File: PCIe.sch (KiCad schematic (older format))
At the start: 16 parts, among them J2 Bus_PCI_Express_Mini, U1 MIMX8MM6DVTLZAA

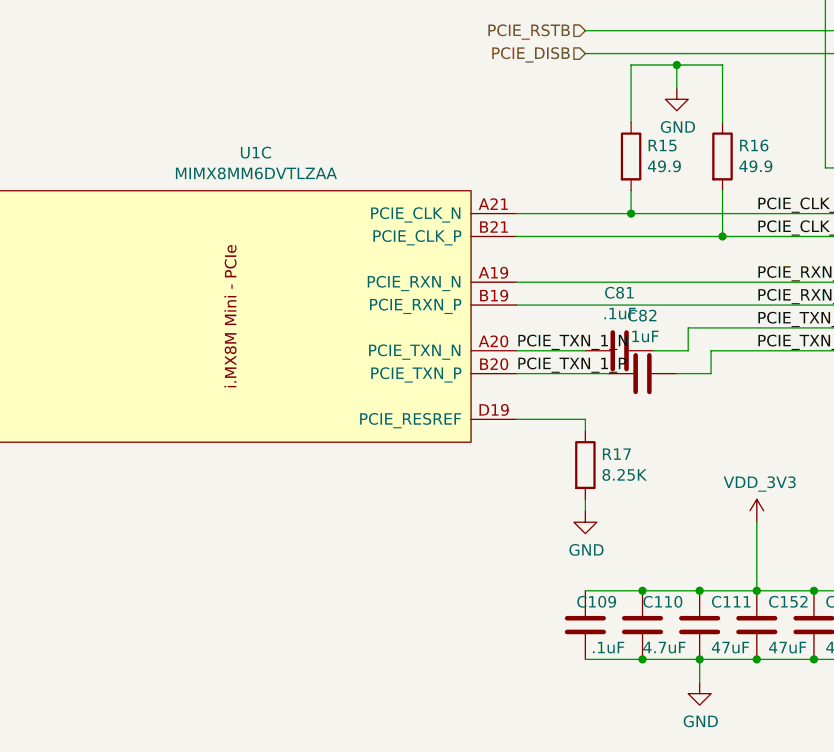
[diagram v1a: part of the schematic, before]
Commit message: Complete entry of bom
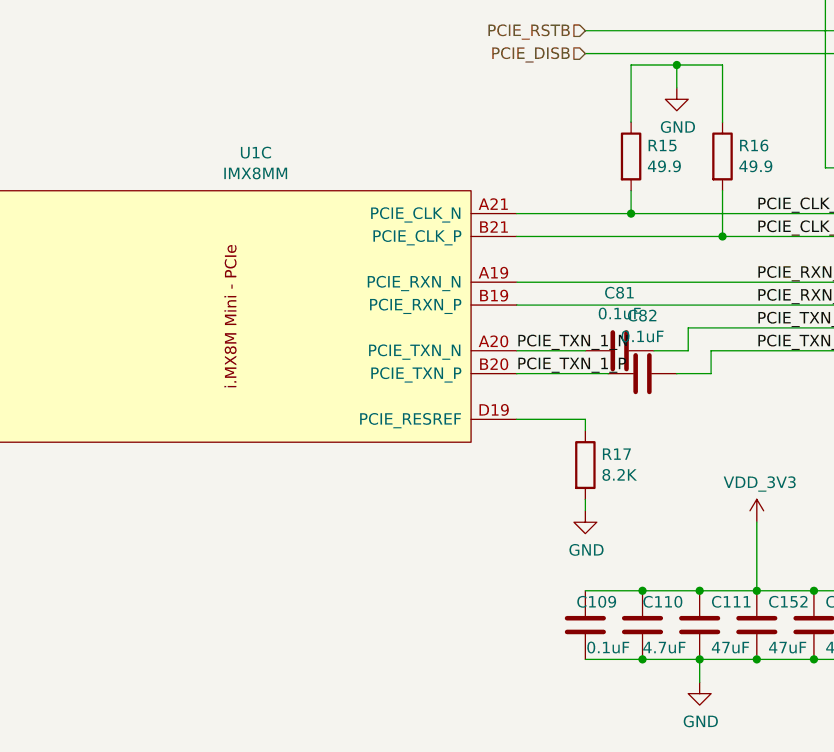
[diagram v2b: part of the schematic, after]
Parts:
- C109, C81, C82: value .1uF -> 0.1uF; footprint Resistor_SMD:R_0201_0603Metric -> Capacitor_SMD:C_0201_0603Metric; Mfgr (none) -> Murata; Part (none) -> GRM033C80J104KE15D; Vendorpart (none) -> 490-10390-1-ND
- C110, C156: Mfgr (none) -> Murata; Part (none) -> GRM155C80J475MEAAD; Vendorpart (none) -> 490-14458-1-ND
- C111, C152, C153, C154, C155: Mfgr (none) -> Murata; Part (none) -> GRM21BC80G476ME15L; Vendorpart (none) -> 490-9954-1-ND
- C157: Mfgr (none) -> Murata; Part (none) -> GRM155C80J106ME11D; Vendorpart (none) -> 490-13233-1-ND
- J2: Mfgr (none) -> TE; Part (none) -> 1775838-2; Vendorpart (none) -> A123340CT-ND
- R15, R16: Mfgr (none) -> Yageo; Part (none) -> RC0201FR-0749R9L; Vendorpart (none) -> YAG2702CT-ND
- R17: value 8.25K -> 8.2K; Mfgr (none) -> Yageo; Part (none) -> RC0201FR-078K2L; Vendorpart (none) -> YAG2353CT-ND
- U1: value MIMX8MM6DVTLZAA -> IMX8MM; Mfgr (none) -> NXP; Part (none) -> MIMX8MM6CVTKZAA; Vendorpart (none) -> 568-15276-ND
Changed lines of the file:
@@
 F 2 "mxenc:1775838-2-NPTH" H 7350 3750 50  0001 C CNN
 F 3 "~" H 7200 2600 50  0001 C CNN
+F 4 "TE" H 7350 3750 50  0001 C CNN "Mfgr"
+F 5 "1775838-2" H 7350 3750 50  0001 C CNN "Part"
+F 6 "A123340CT-ND" H 7350 3750 50  0001 C CNN "Vendorpart"
 	1    7350 3750
 	1    0    0    1
@@
 P 3700 6150
 F 0 "U1" H 3808 9015 50  0000 C CNN
-F 1 "MIMX8MM6DVTLZAA" H 3808 8924 50  0000 C CNN
+F 1 "IMX8MM" H 3808 8924 50  0000 C CNN
 F 2 "mxenc:BGA-729_27x27_14.0x14.0mm" H 3950 8900 50  0001 C CNN
 F 3 "" H 2950 8900 50  0001 C CNN
+F 4 "NXP" H 3700 6150 50  0001 C CNN "Mfgr"
+F 5 "MIMX8MM6CVTKZAA" H 3700 6150 50  0001 C CNN "Part"
+F 6 "568-15276-ND" H 3700 6150 50  0001 C CNN "Vendorpart"
 	3    3700 6150
 	1    0    0    -1
@@
 P 5250 4650
 F 0 "R17" H 5320 4696 50  0000 L CNN
-F 1 "8.25K" H 5320 4605 50  0000 L CNN
+F 1 "8.2K" H 5320 4605 50  0000 L CNN
 F 2 "Resistor_SMD:R_0201_0603Metric" V 5180 4650 50  0001 C CNN
 F 3 "~" H 5250 4650 50  0001 C CNN
+F 4 "Yageo" H 5250 4650 50  0001 C CNN "Mfgr"
+F 5 "RC0201FR-078K2L" H 5250 4650 50  0001 C CNN "Part"
+F 6 "YAG2353CT-ND" H 5250 4650 50  0001 C CNN "Vendorpart"
 	1    5250 4650
 	1    0    0    -1
@@
 F 2 "Resistor_SMD:R_0201_0603Metric" V 5380 3300 50  0001 C CNN
 F 3 "~" H 5450 3300 50  0001 C CNN
+F 4 "Yageo" H 5450 3300 50  0001 C CNN "Mfgr"
+F 5 "RC0201FR-0749R9L" H 5450 3300 50  0001 C CNN "Part"
+F 6 "YAG2702CT-ND" H 5450 3300 50  0001 C CNN "Vendorpart"
 	1    5450 3300
 	1    0    0    -1
@@
 F 2 "Resistor_SMD:R_0201_0603Metric" V 5780 3300 50  0001 C CNN
 F 3 "~" H 5850 3300 50  0001 C CNN
+F 4 "Yageo" H 5850 3300 50  0001 C CNN "Mfgr"
+F 5 "RC0201FR-0749R9L" H 5850 3300 50  0001 C CNN "Part"
+F 6 "YAG2702CT-ND" H 5850 3300 50  0001 C CNN "Vendorpart"
 	1    5850 3300
 	1    0    0    -1
@@
 F 2 "Capacitor_SMD:C_0402_1005Metric" H 7938 5200 50  0001 C CNN
 F 3 "~" H 7900 5350 50  0001 C CNN
+F 4 "Murata" H 7900 5350 50  0001 C CNN "Mfgr"
+F 5 "GRM155C80J475MEAAD" H 7900 5350 50  0001 C CNN "Part"
+F 6 "490-14458-1-ND" H 7900 5350 50  0001 C CNN "Vendorpart"
 	1    7900 5350
 	1    0    0    -1
@@
 F 2 "Capacitor_SMD:C_0402_1005Metric" H 8188 5200 50  0001 C CNN
 F 3 "~" H 8150 5350 50  0001 C CNN
+F 4 "Murata" H 8150 5350 50  0001 C CNN "Mfgr"
+F 5 "GRM155C80J106ME11D" H 8150 5350 50  0001 C CNN "Part"
+F 6 "490-13233-1-ND" H 8150 5350 50  0001 C CNN "Vendorpart"
 	1    8150 5350
 	1    0    0    -1
@@
 F 2 "Capacitor_SMD:C_0805_2012Metric" H 6788 5200 50  0001 C CNN
 F 3 "~" H 6750 5350 50  0001 C CNN
+F 4 "Murata" H 6750 5350 50  0001 C CNN "Mfgr"
+F 5 "GRM21BC80G476ME15L" H 6750 5350 50  0001 C CNN "Part"
+F 6 "490-9954-1-ND" H 6750 5350 50  0001 C CNN "Vendorpart"
 	1    6750 5350
 	1    0    0    -1
@@
 F 2 "Capacitor_SMD:C_0805_2012Metric" H 6538 5200 50  0001 C CNN
 F 3 "~" H 6500 5350 50  0001 C CNN
+F 4 "Murata" H 6500 5350 50  0001 C CNN "Mfgr"
+F 5 "GRM21BC80G476ME15L" H 6500 5350 50  0001 C CNN "Part"
+F 6 "490-9954-1-ND" H 6500 5350 50  0001 C CNN "Vendorpart"
 	1    6500 5350
 	1    0    0    -1
@@
 F 2 "Capacitor_SMD:C_0805_2012Metric" H 6288 5200 50  0001 C CNN
 F 3 "~" H 6250 5350 50  0001 C CNN
+F 4 "Murata" H 6250 5350 50  0001 C CNN "Mfgr"
+F 5 "GRM21BC80G476ME15L" H 6250 5350 50  0001 C CNN "Part"
+F 6 "490-9954-1-ND" H 6250 5350 50  0001 C CNN "Vendorpart"
 	1    6250 5350
 	1    0    0    -1
@@
 F 2 "Capacitor_SMD:C_0805_2012Metric" H 6038 5200 50  0001 C CNN
 F 3 "~" H 6000 5350 50  0001 C CNN
+F 4 "Murata" H 6000 5350 50  0001 C CNN "Mfgr"
+F 5 "GRM21BC80G476ME15L" H 6000 5350 50  0001 C CNN "Part"
+F 6 "490-9954-1-ND" H 6000 5350 50  0001 C CNN "Vendorpart"
 	1    6000 5350
 	1    0    0    -1
@@
 F 2 "Capacitor_SMD:C_0805_2012Metric" H 5788 5200 50  0001 C CNN
 F 3 "~" H 5750 5350 50  0001 C CNN
+F 4 "Murata" H 5750 5350 50  0001 C CNN "Mfgr"
+F 5 "GRM21BC80G476ME15L" H 5750 5350 50  0001 C CNN "Part"
+F 6 "490-9954-1-ND" H 5750 5350 50  0001 C CNN "Vendorpart"
 	1    5750 5350
 	1    0    0    -1
@@
 F 2 "Capacitor_SMD:C_0402_1005Metric" H 5538 5200 50  0001 C CNN
 F 3 "~" H 5500 5350 50  0001 C CNN
+F 4 "Murata" H 5500 5350 50  0001 C CNN "Mfgr"
+F 5 "GRM155C80J475MEAAD" H 5500 5350 50  0001 C CNN "Part"
+F 6 "490-14458-1-ND" H 5500 5350 50  0001 C CNN "Vendorpart"
 	1    5500 5350
 	1    0    0    -1
@@
 P 5250 5350
 F 0 "C109" H 5300 5450 50  0000 C CNN
-F 1 ".1uF" H 5350 5250 50  0000 C CNN
-F 2 "Resistor_SMD:R_0201_0603Metric" H 5288 5200 50  0001 C CNN
+F 1 "0.1uF" H 5350 5250 50  0000 C CNN
+F 2 "Capacitor_SMD:C_0201_0603Metric" H 5288 5200 50  0001 C CNN
 F 3 "~" H 5250 5350 50  0001 C CNN
+F 4 "Murata" H 5250 5350 50  0001 C CNN "Mfgr"
+F 5 "GRM033C80J104KE15D" H 5250 5350 50  0001 C CNN "Part"
+F 6 "490-10390-1-ND" H 5250 5350 50  0001 C CNN "Vendorpart"
 	1    5250 5350
 	1    0    0    -1
@@
 P 5500 4250
 F 0 "C82" V 5248 4250 50  0000 C CNN
-F 1 ".1uF" V 5339 4250 50  0000 C CNN
-F 2 "Resistor_SMD:R_0201_0603Metric" H 5538 4100 50  0001 C CNN
+F 1 "0.1uF" V 5339 4250 50  0000 C CNN
+F 2 "Capacitor_SMD:C_0201_0603Metric" H 5538 4100 50  0001 C CNN
 F 3 "~" H 5500 4250 50  0001 C CNN
+F 4 "Murata" H 5500 4250 50  0001 C CNN "Mfgr"
+F 5 "GRM033C80J104KE15D" H 5500 4250 50  0001 C CNN "Part"
+F 6 "490-10390-1-ND" H 5500 4250 50  0001 C CNN "Vendorpart"
 	1    5500 4250
 	0    1    1    0
@@
 P 5400 4150
 F 0 "C81" V 5148 4150 50  0000 C CNN
-F 1 ".1uF" V 5239 4150 50  0000 C CNN
-F 2 "Resistor_SMD:R_0201_0603Metric" H 5438 4000 50  0001 C CNN
+F 1 "0.1uF" V 5239 4150 50  0000 C CNN
+F 2 "Capacitor_SMD:C_0201_0603Metric" H 5438 4000 50  0001 C CNN
 F 3 "~" H 5400 4150 50  0001 C CNN
+F 4 "Murata" H 5400 4150 50  0001 C CNN "Mfgr"
+F 5 "GRM033C80J104KE15D" H 5400 4150 50  0001 C CNN "Part"
+F 6 "490-10390-1-ND" H 5400 4150 50  0001 C CNN "Vendorpart"
 	1    5400 4150
 	0    1    1    0

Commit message: Ground mounting pads and route ecspi to expansion
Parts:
- J2: symbol Connector:Bus_PCI_Express_Mini -> mxenc:Bus_PCI_Express_Mini
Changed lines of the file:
@@
 $EndDescr
 $Comp
-L Connector:Bus_PCI_Express_Mini J?
+L mxenc:Bus_PCI_Express_Mini J?
 U 1 1 5D31B8E0
 P 7350 3750

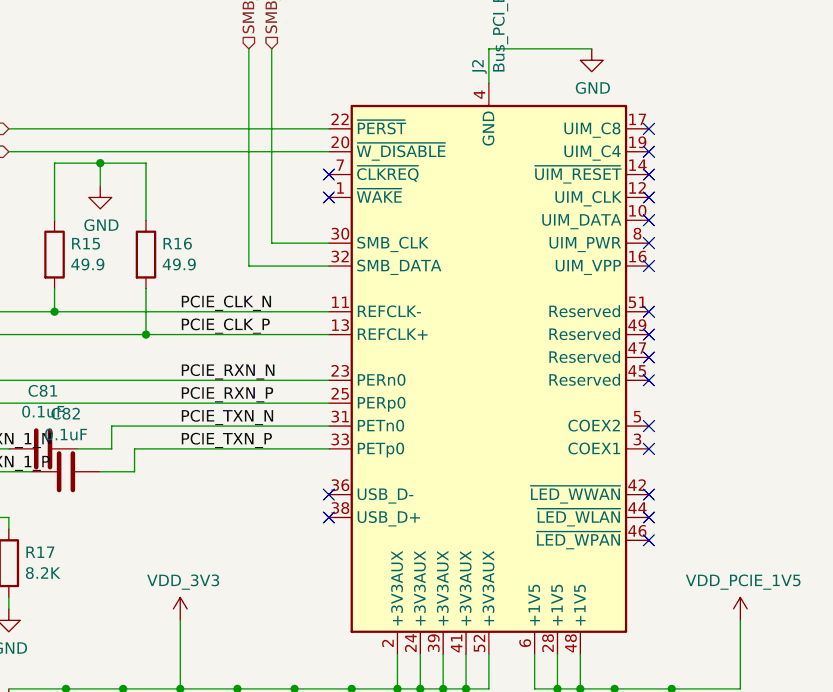
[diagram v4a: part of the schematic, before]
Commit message: UIM and USB routing for PCIE to expansion
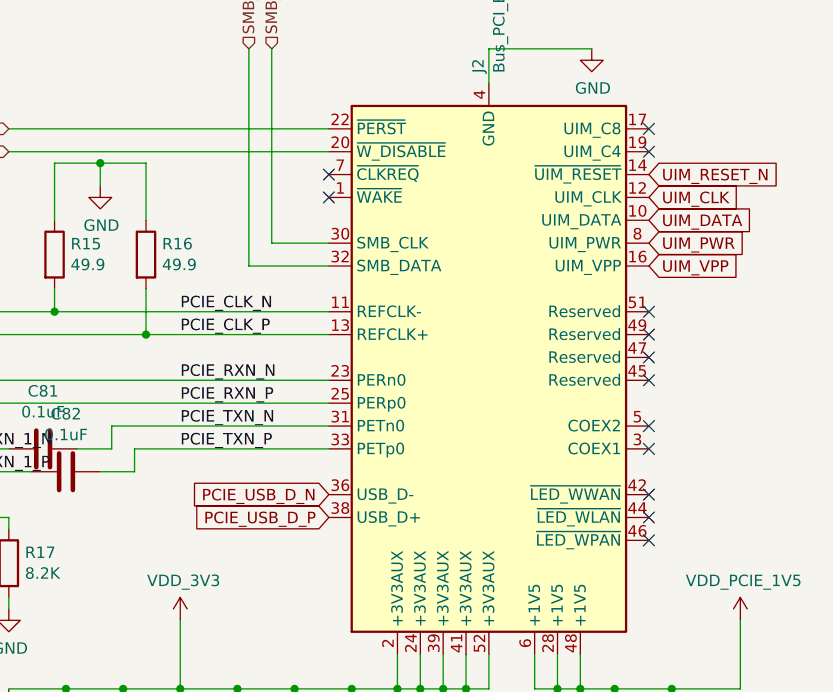
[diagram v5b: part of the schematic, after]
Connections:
- net UIM_DATA: now reaches J2.10 (UIM_DATA)
- net UIM_CLK: now reaches J2.12 (UIM_CLK)
- net UIM_RESET_N: now reaches J2.14 (~UIM_RESET)
- net UIM_VPP: now reaches J2.16 (UIM_VPP)
- net PCIE_USB_D_N: now reaches J2.36 (USB_D-)
- net PCIE_USB_D_P: now reaches J2.38 (USB_D+)
- net UIM_PWR: now reaches J2.8 (UIM_PWR)
- no-connect marks 20 -> 13
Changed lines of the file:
@@
 Wire Wire Line
 	7350 2400 7350 2550
-NoConn ~ 8050 2750
-NoConn ~ 8050 2850
 Wire Wire Line
 	5250 2850 6650 2850
@@
 NoConn ~ 6650 2950
 NoConn ~ 6650 3050
-NoConn ~ 6650 4350
-NoConn ~ 6650 4450
-NoConn ~ 8050 2950
-NoConn ~ 8050 3050
-NoConn ~ 8050 3150
-NoConn ~ 8050 3250
-NoConn ~ 8050 3350
 $Comp
 L power:GND #PWR0198
@@
 Text HLabel 5250 2750 0    50   Input ~ 0
 PCIE_RSTB
+NoConn ~ 8050 2750
+NoConn ~ 8050 2850
+Text GLabel 8050 2950 2    50   Input ~ 0
+UIM_RESET_N
+Text GLabel 8050 3050 2    50   Input ~ 0
+UIM_CLK
+Text GLabel 8050 3150 2    50   Input ~ 0
+UIM_DATA
+Text GLabel 8050 3250 2    50   Input ~ 0
+UIM_PWR
+Text GLabel 8050 3350 2    50   Input ~ 0
+UIM_VPP
+Text GLabel 6650 4350 0    50   Input ~ 0
+PCIE_USB_D_N
+Text GLabel 6650 4450 0    50   Input ~ 0
+PCIE_USB_D_P
 $EndSCHEMATC

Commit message: Additional capacitance for PCIe to support high power modules
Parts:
- C111, C152, C153: value 47uF -> 220uF; footprint Capacitor_SMD:C_0805_2012Metric -> Capacitor_SMD:C_1206_3216Metric; Part GRM21BC80G476ME15L -> GRM31CR60J227ME11L; Vendorpart 490-9954-1-ND -> 490-13970-1-ND
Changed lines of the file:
@@
 P 6250 5350
 F 0 "C153" H 6300 5450 50  0000 L CNN
-F 1 "47uF" H 6300 5250 50  0000 L CNN
-F 2 "Capacitor_SMD:C_0805_2012Metric" H 6288 5200 50  0001 C CNN
+F 1 "220uF" H 6300 5250 50  0000 L CNN
+F 2 "Capacitor_SMD:C_1206_3216Metric" H 6288 5200 50  0001 C CNN
 F 3 "~" H 6250 5350 50  0001 C CNN
 F 4 "Murata" H 6250 5350 50  0001 C CNN "Mfgr"
-F 5 "GRM21BC80G476ME15L" H 6250 5350 50  0001 C CNN "Part"
-F 6 "490-9954-1-ND" H 6250 5350 50  0001 C CNN "Vendorpart"
+F 5 "GRM31CR60J227ME11L" H 6250 5350 50  0001 C CNN "Part"
+F 6 "490-13970-1-ND" H 6250 5350 50  0001 C CNN "Vendorpart"
 	1    6250 5350
 	1    0    0    -1
@@
 P 6000 5350
 F 0 "C152" H 6050 5450 50  0000 L CNN
-F 1 "47uF" H 6050 5250 50  0000 L CNN
-F 2 "Capacitor_SMD:C_0805_2012Metric" H 6038 5200 50  0001 C CNN
+F 1 "220uF" H 6050 5250 50  0000 L CNN
+F 2 "Capacitor_SMD:C_1206_3216Metric" H 6038 5200 50  0001 C CNN
 F 3 "~" H 6000 5350 50  0001 C CNN
 F 4 "Murata" H 6000 5350 50  0001 C CNN "Mfgr"
-F 5 "GRM21BC80G476ME15L" H 6000 5350 50  0001 C CNN "Part"
-F 6 "490-9954-1-ND" H 6000 5350 50  0001 C CNN "Vendorpart"
+F 5 "GRM31CR60J227ME11L" H 6000 5350 50  0001 C CNN "Part"
+F 6 "490-13970-1-ND" H 6000 5350 50  0001 C CNN "Vendorpart"
 	1    6000 5350
 	1    0    0    -1
@@
 P 5750 5350
 F 0 "C111" H 5800 5450 50  0000 L CNN
-F 1 "47uF" H 5800 5250 50  0000 L CNN
-F 2 "Capacitor_SMD:C_0805_2012Metric" H 5788 5200 50  0001 C CNN
+F 1 "220uF" H 5800 5250 50  0000 L CNN
+F 2 "Capacitor_SMD:C_1206_3216Metric" H 5788 5200 50  0001 C CNN
 F 3 "~" H 5750 5350 50  0001 C CNN
 F 4 "Murata" H 5750 5350 50  0001 C CNN "Mfgr"
-F 5 "GRM21BC80G476ME15L" H 5750 5350 50  0001 C CNN "Part"
-F 6 "490-9954-1-ND" H 5750 5350 50  0001 C CNN "Vendorpart"
+F 5 "GRM31CR60J227ME11L" H 5750 5350 50  0001 C CNN "Part"
+F 6 "490-13970-1-ND" H 5750 5350 50  0001 C CNN "Vendorpart"
 	1    5750 5350
 	1    0    0    -1

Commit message: Added zener for tvs on pcie
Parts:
- added D9: 5.1V, Diode_SMD:D_SOD-523, symbol Device:D_Zener
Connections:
- net GND: now also D9.2 (A)
- net VDD_3V3: now also D9.1 (K)
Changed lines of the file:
@@
 Text GLabel 6650 4450 0    50   Input ~ 0
 PCIE_USB_D_P
+$Comp
+L Device:D_Zener D9
+U 1 1 5ECE4766
+P 5050 5350
+F 0 "D9" V 4959 5271 50  0000 R CNN
+F 1 "5.1V" V 5050 5271 50  0000 R CNN
+F 2 "Diode_SMD:D_SOD-523" H 5050 5350 50  0001 C CNN
+F 3 "~" H 5050 5350 50  0001 C CNN
+F 4 "MM5Z5V1T1GOSCT-ND" V 5141 5271 50  0000 R CNN "Vendorpart"
+F 5 "On Semi" H 5050 5350 50  0001 C CNN "Mfgr"
+F 6 "MM5Z5V1T1G" H 5050 5350 50  0001 C CNN "Part"
+	1    5050 5350
+	0    1    1    0
+$EndComp
+Wire Wire Line
+	5250 5200 5050 5200
+Connection ~ 5250 5200
+Wire Wire Line
+	5050 5500 5250 5500
+Connection ~ 5250 5500
 $EndSCHEMATC
